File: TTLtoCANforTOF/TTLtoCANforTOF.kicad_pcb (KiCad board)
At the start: 2 copper layers, 28.6 x 24.8 mm, 44 parts, among them J1 CAN, J2 STP-23L, J4 XT30, J5 SWD, SW1 SW_SPST, U1 TPS54202DDC, U2 ME6211C33M5, U3 STM32G0B1CBTx, U6 TCAN3413DR, Y1 X32258MSB

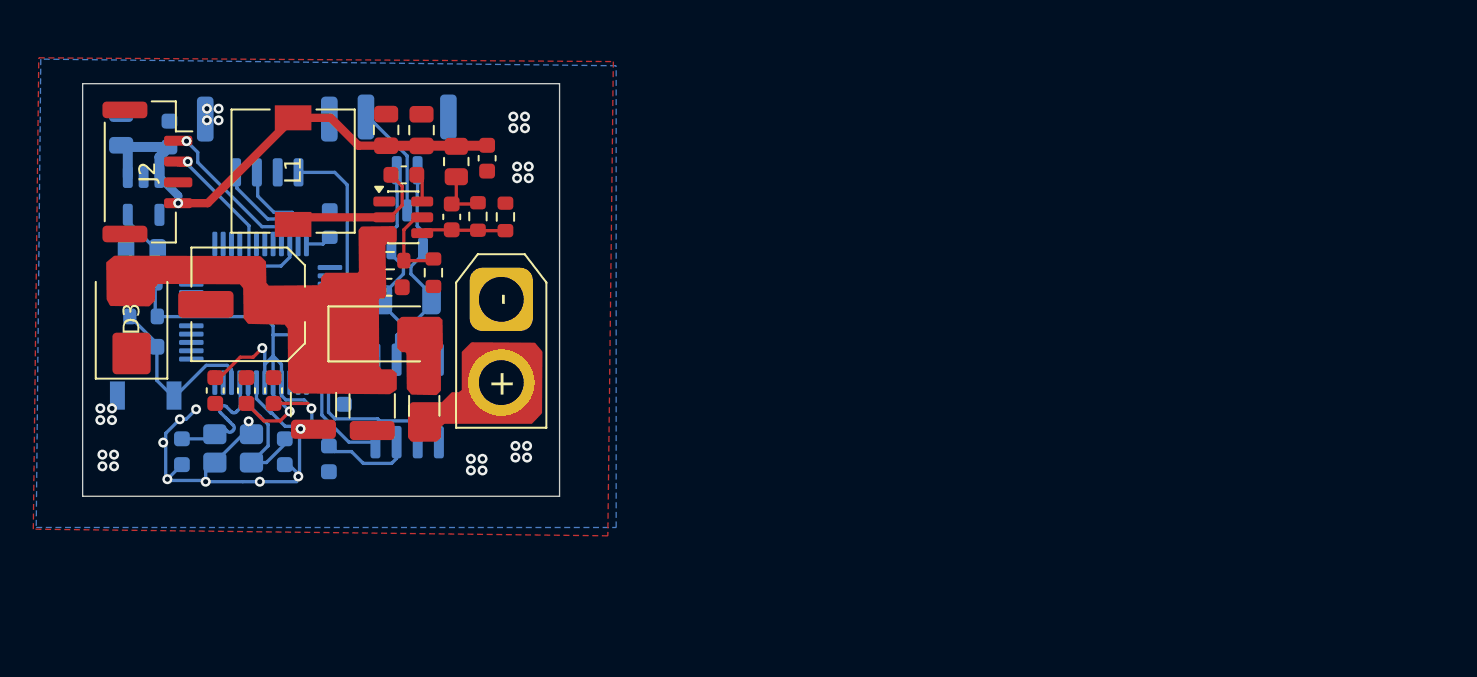
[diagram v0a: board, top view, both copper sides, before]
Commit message: 修改了保护电路
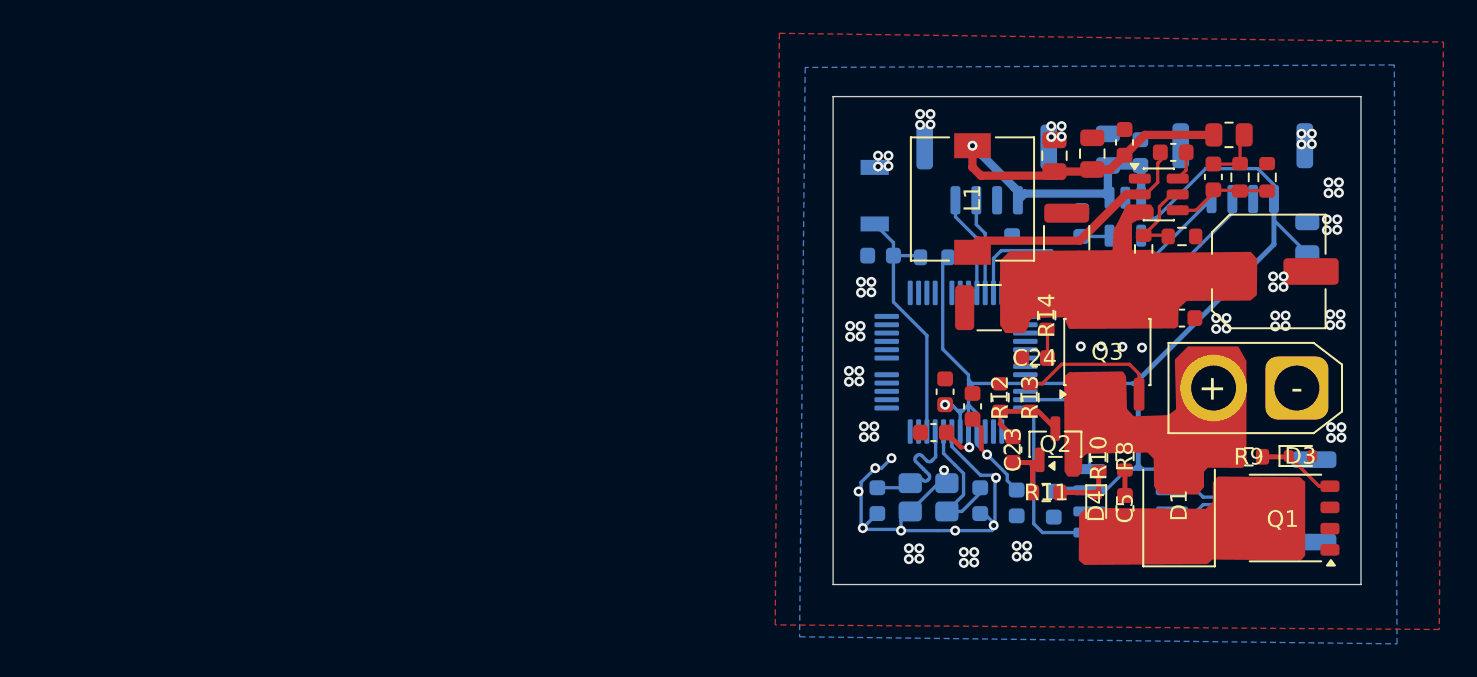
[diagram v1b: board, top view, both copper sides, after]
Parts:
- removed D2: SS310, Diode_SMD:D_SMA
- removed F1: BSMD1206-100-60V, Fuse:Fuse_1206_3216Metric
- removed J1: CAN, Connector_JST:JST_GH_SM02B-GHS-TB_1x02-1MP_P1.25mm_Horizontal
- removed J5: SWD, Connector_Molex:Molex_CLIK-Mate_502386-0470_1x04-1MP_P1.25mm_Horizontal
- added C23: 100nF, Capacitor_SMD:C_0603_1608Metric, F.Cu at (108.5, 51.7)
- added C24: 10nF, Capacitor_SMD:C_0603_1608Metric, F.Cu at (109.8, 46.2)
- added C5: 10nF, Capacitor_SMD:C_0603_1608Metric, F.Cu at (115.3, 55.2)
- added D4: 28-32V, Diode_SMD:D_SOD-523, F.Cu at (113.5, 55.1)
- added J3: TOF, Connector_JST:JST_GH_SM04B-GHS-TB_1x04-1MP_P1.25mm_Horizontal, B.Cu at (107.0, 34.9)
- added J6: SWD, Connector_Molex:Molex_CLIK-Mate_502386-0470_1x04-1MP_P1.25mm_Horizontal, B.Cu at (122.3, 34.8)
- added Q1: PSMN1R4-40YLD, Package_TO_SOT_SMD:LFPAK56, F.Cu at (124.9, 55.8)
- added Q2: Q_PNP, Package_TO_SOT_SMD:SOT-23, F.Cu at (111.1, 51.4)
- added Q3: AO4485, Package_SO:SOP-8_3.76x4.96mm_P1.27mm, F.Cu at (114.2, 45.9)
- added R10: 100K, Resistor_SMD:R_0603_1608Metric, F.Cu at (113.7, 52.2)
- added R11: 1K, Resistor_SMD:R_0603_1608Metric, F.Cu at (110.5, 54.3)
- added R12: 10K, Resistor_SMD:R_0603_1608Metric, F.Cu at (107.8, 48.6)
- added R13: 1K, Resistor_SMD:R_0603_1608Metric, F.Cu at (109.6, 48.6)
- added R14: 33R, Resistor_SMD:R_0603_1608Metric, F.Cu at (110.6, 43.7)
- added R9: 100K, Resistor_SMD:R_0603_1608Metric, F.Cu at (122.7, 52.2)
- D1: value ESDCAN01-2BLY -> SMBJ30CA; footprint Package_TO_SOT_SMD:SOT-23-3 -> Diode_SMD:D_SMB; moved to F.Cu
- D3: value SMBJ24CA -> BZX584C9V1; footprint Diode_SMD:D_SMB -> Diode_SMD:D_SOD-523
- J2: value STP-23L -> CAN; footprint Connector_JST:JST_GH_SM04B-GHS-TB_1x04-1MP_P1.25mm_Horizontal -> Connector_JST:JST_GH_SM02B-GHS-TB_1x02-1MP_P1.25mm_Horizontal; moved to B.Cu
- R8: value 120Ω -> 33R; footprint Resistor_SMD:R_1206_3216Metric -> Resistor_SMD:R_0603_1608Metric; moved to F.Cu
- moved J2 71.5 mm to (125.3, 54.8)
- moved D3 70.7 mm to (125.8, 52.1), turned to 0 degrees
- moved C11 70.0 mm to (126.2, 39.0), turned to 90 degrees
- moved C22 61.3 mm to (123.9, 41.0), turned to 0 degrees
- moved C9 59.3 mm to (114.2, 33.7)
- moved U2 59.0 mm to (115.3, 37.7)
- moved C10 58.3 mm to (116.2, 33.9)
- moved C12 56.5 mm to (112.7, 38.1), turned to 90 degrees
- moved D1 49.2 mm to (118.5, 55.1)
- moved J4 48.1 mm to (125.6, 48.0), turned to 180 degrees
- moved C2 47.6 mm to (118.7, 43.8)
- moved R6 47.6 mm to (103.8, 40.2)
- moved R3 46.4 mm to (121.5, 32.8), turned to 0 degrees
- moved C1 46.2 mm to (118.2, 33.9)
- moved R4 45.8 mm to (122.2, 35.4)
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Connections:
- D1 pad 1: /CAN+ -> GND_IN
- D1 pad 2: /CAN- -> VCC_IN
- D3 pad 1: GND -> Net-(D3-K)
- D3 pad 2: +24V -> GND
- J2 pad 1: /USART1_TX -> /CAN-
- J2 pad 2: /USART1_RX -> /CAN+
- J4 pad 2: Net-(J4-Pin_2) -> VCC_IN
- R8 pad 1: /CAN+ -> VCC_IN
- R8 pad 2: /CAN- -> Net-(C5-Pad1)
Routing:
- net +3.3V: track 67.1 -> 84.7 mm
- net /SWCLK: track 7.74 -> 18.8 mm
- net /SWDIO: track 6.09 -> 17.0 mm
- net Net-(Q3-G): track 0.00 -> 8.50 mm
- net /CAN-: track 13.0 -> 5.66 mm
- net /CAN+: track 13.0 -> 5.66 mm
- net GND: track 34.0 -> 27.3 mm, vias 37 -> 85
- net /USART1_RX: track 12.2 -> 5.78 mm, vias 1 -> 0
- net Net-(U1-SW): track 9.13 -> 14.8 mm
- net Net-(C23-Pad2): track 0.00 -> 5.60 mm
- net Net-(D3-K): track 0.00 -> 4.82 mm
- net /NRST: track 11.0 -> 15.4 mm
- net Net-(C23-Pad1): track 0.00 -> 4.10 mm
- net Net-(D4-K): track 0.00 -> 3.66 mm
- net 5V: track 29.9 -> 33.4 mm
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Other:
- board size 28.6 x 24.8 mm -> 31.7 x 29.3 mm
